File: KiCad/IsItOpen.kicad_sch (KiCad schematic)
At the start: 49 parts, among them J1 SPI Header, SW1 SW_Push, SW2 SW_Push, SW3 SW_Push, SW4 SW_Push, U1 ESP32-DevKitC, U2 MCP4801, U3 LM4562, U4 LM4871

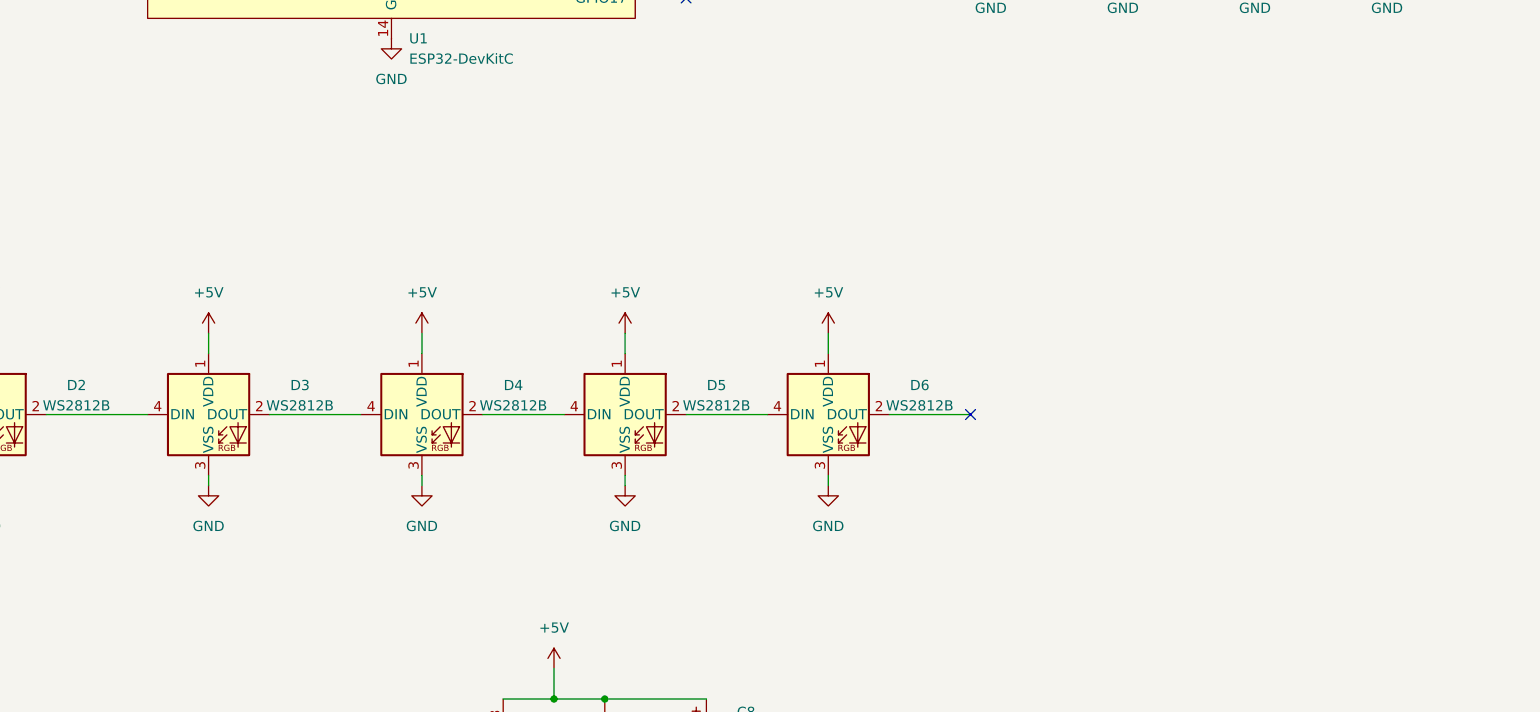
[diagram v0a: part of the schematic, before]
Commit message: added pcb connector
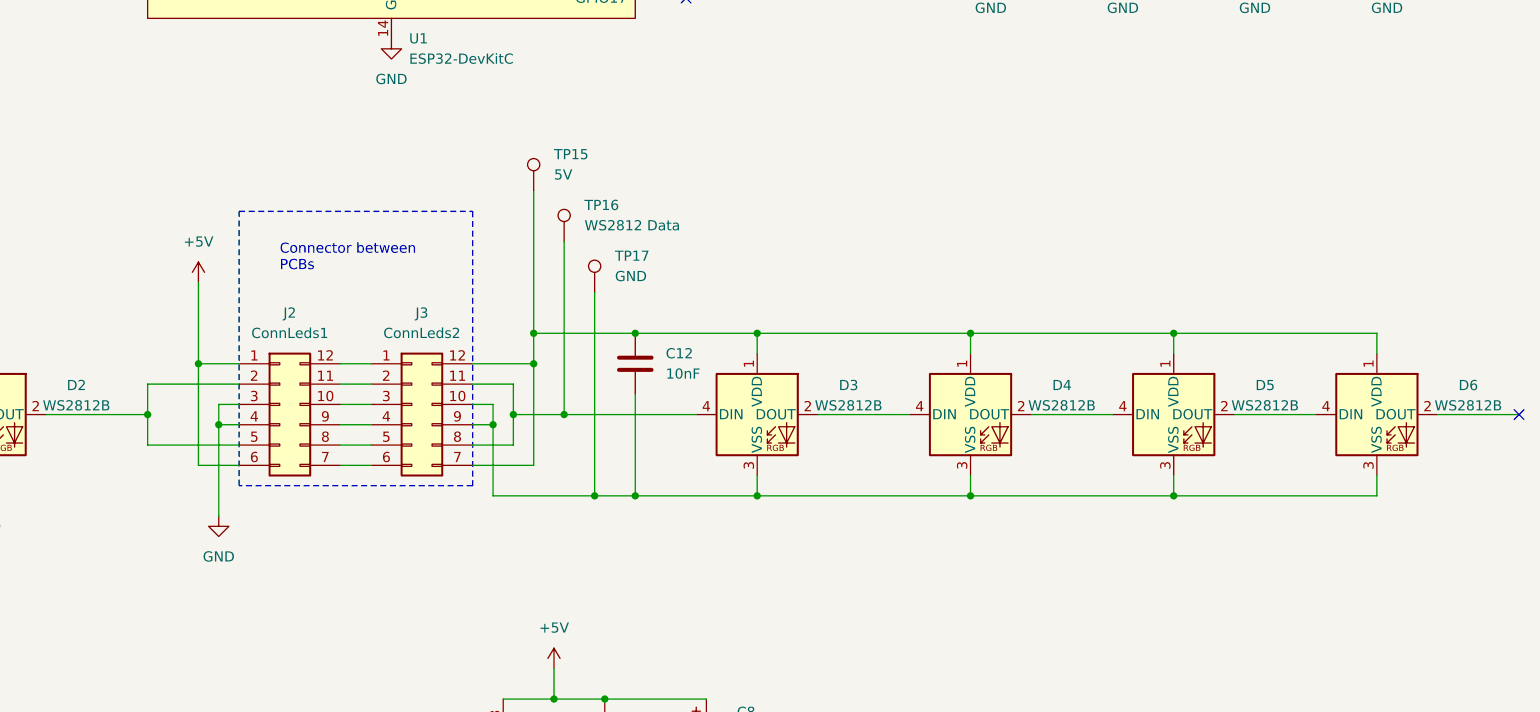
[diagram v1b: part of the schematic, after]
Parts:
- added C12: 10nF, Capacitor_SMD:C_1206_3216Metric_Pad1.33x1.80mm_HandSolder, symbol Device:C
- added J2: ConnLeds1, symbol Connector_Generic:Conn_02x06_Counter_Clockwise
- added J3: ConnLeds2, symbol Connector_Generic:Conn_02x06_Counter_Clockwise
- added TP15: 5V, TestPoint:TestPoint_Pad_D3.0mm, symbol Connector:TestPoint
- added TP16: WS2812 Data, TestPoint:TestPoint_Pad_D3.0mm, symbol Connector:TestPoint
- added TP17: GND, TestPoint:TestPoint_Pad_D3.0mm, symbol Connector:TestPoint
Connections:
- net +5V: now also J2.1 (Pin_1), J2.6 (Pin_6); no longer D3.1 (VDD), D4.1 (VDD), D5.1 (VDD), D6.1 (VDD)
- net GND: now also J2.3 (Pin_3), J2.4 (Pin_4); no longer D3.3 (VSS), D4.3 (VSS), D5.3 (VSS), D6.3 (VSS)
- net at D3.4 (DIN): now also J3.11 (Pin_11), J3.8 (Pin_8), TP16.1; no longer D2.2 (DOUT)
- new net: J2.12 (Pin_12), J3.1 (Pin_1)
- new net: C12.2, D3.3 (VSS), D4.3 (VSS), D5.3 (VSS), D6.3 (VSS), J3.10 (Pin_10), J3.9 (Pin_9), TP17.1
- new net: C12.1, D3.1 (VDD), D4.1 (VDD), D5.1 (VDD), D6.1 (VDD), J3.12 (Pin_12), J3.7 (Pin_7), TP15.1
- new net: J2.11 (Pin_11), J3.2 (Pin_2)
- new net: J2.10 (Pin_10), J3.3 (Pin_3)
- new net: J2.9 (Pin_9), J3.4 (Pin_4)
- new net: J2.8 (Pin_8), J3.5 (Pin_5)
- new net: J2.7 (Pin_7), J3.6 (Pin_6)
- new net: D2.2 (DOUT), J2.2 (Pin_2), J2.5 (Pin_5)
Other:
- note added: "Connector between PCBs"
- moved on the sheet: D3, D4, D5, D6

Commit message: added footprint for pcb connector
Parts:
- removed J2: ConnLeds1, symbol Connector_Generic:Conn_02x06_Counter_Clockwise
- removed J3: ConnLeds2, symbol Connector_Generic:Conn_02x06_Counter_Clockwise
- added J2: Base_Conn, Library:BasePCB, symbol Connector_Generic:Conn_01x06
- added J3: LED_Conn, Library:LedPCB, symbol Connector_Generic:Conn_01x06
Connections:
- net +5V: now also J2.1 (Pin_1), J2.6 (Pin_6)
- net GND: now also J2.3 (Pin_3), J2.4 (Pin_4)
- net at C12.2, D3.3 (VSS), D4.3 (VSS)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: now also J3.3 (Pin_3), J3.4 (Pin_4)
- net at D3.4 (DIN), TP16.1: now also J3.2 (Pin_2), J3.5 (Pin_5)
- net at C12.1, D3.1 (VDD), D4.1 (VDD)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: now also J3.1 (Pin_1), J3.6 (Pin_6)
- net at D2.2 (DOUT): now also J2.2 (Pin_2), J2.5 (Pin_5)
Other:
- company: (none) -> FsInf
- title: (none) -> FsInf Control

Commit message: added basic pcb layout
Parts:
- added H1, H2, H3, H4: MountingHole, MountingHole:MountingHole_3.2mm_M3, symbol Mechanical:MountingHole
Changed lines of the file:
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@@
+    )
+  )
+  (symbol (lib_id "Mechanical:MountingHole") (at 262.89 27.94 0) (unit 1)
+    (in_bom yes) (on_board yes) (dnp no) (fields_autoplaced)
+    (property "Reference" "H1" (at 265.43 26.67 0)
+      (effects (font (size 1.27 1.27)) (justify left))
+    )
+    (property "Value" "MountingHole" (at 265.43 29.21 0)
+      (effects (font (size 1.27 1.27)) (justify left))
+    )
+    (property "Footprint" "MountingHole:MountingHole_3.2mm_M3" (at 262.89 27.94 0)
+      (effects (font (size 1.27 1.27)) hide)
+    )
+    (property "Datasheet" "~" (at 262.89 27.94 0)
+      (effects (font (size 1.27 1.27)) hide)
+    )
+    (instances
+      (project "IsItOpen"
+        (path "/a8d496be-86fc-4980-841d-a8780aee3a24"
+          (reference "H1") (unit 1)
+        )
+      )
     )
   )
@@
     )
   )
+  (symbol (lib_id "Mechanical:MountingHole") (at 262.89 17.78 0) (unit 1)
+    (in_bom yes) (on_board yes) (dnp no) (fields_autoplaced)
+    (property "Reference" "H4" (at 265.43 16.51 0)
+      (effects (font (size 1.27 1.27)) (justify left))
+    )
+    (property "Value" "MountingHole" (at 265.43 19.05 0)
+      (effects (font (size 1.27 1.27)) (justify left))
+    )
+    (property "Footprint" "MountingHole:MountingHole_3.2mm_M3" (at 262.89 17.78 0)
+      (effects (font (size 1.27 1.27)) hide)
+    )
+    (property "Datasheet" "~" (at 262.89 17.78 0)
+      (effects (font (size 1.27 1.27)) hide)
+    )
+    (instances
+      (project "IsItOpen"
+        (path "/a8d496be-86fc-4980-841d-a8780aee3a24"
+          (reference "H4") (unit 1)
+        )
+      )
+    )
+  )
   (symbol (lib_id "power:GND") (at 250.19 245.11 0) (unit 1)
     (in_bom yes) (on_board yes) (dnp no) (fields_autoplaced)
@@
         (path "/a8d496be-86fc-4980-841d-a8780aee3a24"
           (reference "R3") (unit 1)
+        )
+      )
+    )
+  )
+  (symbol (lib_id "Mechanical:MountingHole") (at 262.89 33.02 0) (unit 1)
+    (in_bom yes) (on_board yes) (dnp no) (fields_autoplaced)
+    (property "Reference" "H2" (at 265.43 31.75 0)
+      (effects (font (size 1.27 1.27)) (justify left))
+    )
+    (property "Value" "MountingHole" (at 265.43 34.29 0)
+      (effects (font (size 1.27 1.27)) (justify left))
+    )
+    (property "Footprint" "MountingHole:MountingHole_3.2mm_M3" (at 262.89 33.02 0)
+      (effects (font (size 1.27 1.27)) hide)
+    )
+    (property "Datasheet" "~" (at 262.89 33.02 0)
+      (effects (font (size 1.27 1.27)) hide)
+    )
+    (instances
+      (project "IsItOpen"
+        (path "/a8d496be-86fc-4980-841d-a8780aee3a24"
+          (reference "H2") (unit 1)
         )
       )
@@
         )
       )
+    )
+  )
+  (symbol (lib_id "Mechanical:MountingHole") (at 262.89 22.86 0) (unit 1)
+    (in_bom yes) (on_board yes) (dnp no) (fields_autoplaced)
+    (property "Reference" "H3" (at 265.43 21.59 0)
+      (effects (font (size 1.27 1.27)) (justify left))
+    )
+    (property "Value" "MountingHole" (at 265.43 24.13 0)
+      (effects (font (size 1.27 1.27)) (justify left))
+    )
+    (property "Footprint" "MountingHole:MountingHole_3.2mm_M3" (at 262.89 22.86 0)
+      (effects (font (size 1.27 1.27)) hide)
+    )
+    (property "Datasheet" "~" (at 262.89 22.86 0)
+      (effects (font (size 1.27 1.27)) hide)
+    )
+    (instances
+      (project "IsItOpen"
+        (path "/a8d496be-86fc-4980-841d-a8780aee3a24"
+          (reference "H3") (unit 1)
+        )
+      )

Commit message: routed pcbn
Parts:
- added J4: Power, TerminalBlock_MetzConnect:TerminalBlock_MetzConnect_Type055_RT01502HDWU_1x02_P5.00mm_Horizontal, symbol Connector:Screw_Terminal_01x02
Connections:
- net +5V: now also J4.1 (Pin_1)
- net GND: now also J4.2 (Pin_2)
- net at J1.5 (Pin_5): now also U1.12 (MTMS/GPIO14/ADC2_CH6); no longer U1.13 (MTDI/GPIO12/ADC2_CH5)
- net at J1.6 (Pin_6): now also U1.13 (MTDI/GPIO12/ADC2_CH5); no longer U1.15 (MTCK/GPIO13/ADC2_CH4)
- net at J1.7 (Pin_7): now also U1.15 (MTCK/GPIO13/ADC2_CH4); no longer U1.12 (MTMS/GPIO14/ADC2_CH6)
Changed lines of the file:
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@@
+    (stroke (width 0) (type default))
+  )
+  (wire (pts (xy 129.54 66.04) (xy 120.65 66.04))
     (stroke (width 0) (type default))
   )
@@
     (stroke (width 0) (type default))
   )
+  (wire (pts (xy 53.34 30.48) (xy 53.34 33.02))
+    (stroke (width 0) (type default))
+  )
   (wire (pts (xy 93.98 232.41) (xy 107.95 232.41))
     (stroke (width 0) (type default))
@@
     (stroke (width 0) (type default))
   )
+  (wire (pts (xy 120.65 66.04) (xy 120.65 68.58))
+    (stroke (width 0) (type default))
+  )
   (wire (pts (xy 234.95 153.67) (xy 234.95 156.21))
     (stroke (width 0) (type default))
@@
     (stroke (width 0) (type default))
   )
+  (wire (pts (xy 123.19 68.58) (xy 123.19 60.96))
+    (stroke (width 0) (type default))
+  )
   (wire (pts (xy 177.8 163.83) (xy 184.15 163.83))
     (stroke (width 0) (type default))
@@
     (stroke (width 0) (type default))
   )
+  (wire (pts (xy 54.61 35.56) (xy 53.34 35.56))
+    (stroke (width 0) (type default))
+  )
   (wire (pts (xy 195.58 86.36) (xy 278.13 86.36))
     (stroke (width 0) (type default))
@@
     (stroke (width 0) (type default))
   )
+  (wire (pts (xy 118.11 66.04) (xy 110.49 66.04))
+    (stroke (width 0) (type default))
+  )
   (wire (pts (xy 180.34 157.48) (xy 180.34 153.67))
     (stroke (width 0) (type default))
@@
     (stroke (width 0) (type default))
   )
+  (wire (pts (xy 115.57 60.96) (xy 115.57 63.5))
+    (stroke (width 0) (type default))
+  )
   (wire (pts (xy 97.79 207.01) (xy 85.09 207.01))
     (stroke (width 0) (type default))
@@
     (stroke (width 0) (type default))
   )
+  (wire (pts (xy 120.65 68.58) (xy 110.49 68.58))
+    (stroke (width 0) (type default))
+  )
   (wire (pts (xy 177.8 160.02) (xy 177.8 163.83))
     (stroke (width 0) (type default))
   )
+  (wire (pts (xy 123.19 60.96) (xy 115.57 60.96))
+    (stroke (width 0) (type default))
+  )
+  (wire (pts (xy 53.34 33.02) (xy 54.61 33.02))
+    (stroke (width 0) (type default))
+  )
   (wire (pts (xy 163.83 224.79) (xy 153.67 224.79))
     (stroke (width 0) (type default))
@@
     (stroke (width 0) (type default))
   )
-  (wire (pts (xy 110.49 66.04) (xy 129.54 66.04))
-    (stroke (width 0) (type default))
-  )
   (wire (pts (xy 245.11 78.74) (xy 245.11 81.28))
     (stroke (width 0) (type default))
@@
     (stroke (width 0) (type default))
   )
+  (wire (pts (xy 129.54 63.5) (xy 118.11 63.5))
+    (stroke (width 0) (type default))
+  )
   (wire (pts (xy 180.34 153.67) (xy 193.04 153.67))
     (stroke (width 0) (type default))
@@
     (stroke (width 0) (type default))
   )
-  (wire (pts (xy 110.49 63.5) (xy 129.54 63.5))
-    (stroke (width 0) (type default))
-  )
   (wire (pts (xy 217.17 237.49) (xy 217.17 248.92))
     (stroke (width 0) (type default))
@@
     (stroke (width 0) (type default))
   )
+  (wire (pts (xy 115.57 63.5) (xy 110.49 63.5))
+    (stroke (width 0) (type default))
+  )
   (wire (pts (xy 119.38 163.83) (xy 132.08 163.83))
     (stroke (width 0) (type default))
@@
     (stroke (width 0) (type default))
   )
+  (wire (pts (xy 118.11 63.5) (xy 118.11 66.04))
+    (stroke (width 0) (type default))
+  )
   (wire (pts (xy 132.08 160.02) (xy 132.08 163.83))
     (stroke (width 0) (type default))
@@
     (stroke (width 0) (type default))
   )
-  (wire (pts (xy 110.49 68.58) (xy 129.54 68.58))
-    (stroke (width 0) (type default))
-  )
   (wire (pts (xy 189.23 207.01) (xy 201.93 207.01))
     (stroke (width 0) (type default))
@@
     (stroke (width 0) (type default))
   )
+  (wire (pts (xy 53.34 35.56) (xy 53.34 38.1))
+    (stroke (width 0) (type default))
+  )
   (wire (pts (xy 260.35 153.67) (xy 260.35 156.21))
+    (stroke (width 0) (type default))
+  )
+  (wire (pts (xy 129.54 68.58) (xy 123.19 68.58))
     (stroke (width 0) (type default))
   )
@@
         (path "/a8d496be-86fc-4980-841d-a8780aee3a24"
           (reference "#PWR035") (unit 1)
+        )
+      )
+    )
+  )
+  (symbol (lib_id "Connector:Screw_Terminal_01x02") (at 59.69 33.02 0) (unit 1)
+    (in_bom yes) (on_board yes) (dnp no) (fields_autoplaced)
+    (property "Reference" "J4" (at 62.23 33.02 0)
+      (effects (font (size 1.27 1.27)) (justify left))
+    )
+    (property "Value" "Power" (at 62.23 35.56 0)
+      (effects (font (size 1.27 1.27)) (justify left))
+    )
+    (property "Footprint" "TerminalBlock_MetzConnect:TerminalBlock_MetzConnect_Type055_RT01502HDWU_1x02_P5.00mm_Horizontal" (at 59.69 33.02 0)
+      (effects (font (size 1.27 1.27)) hide)
+    )
+    (property "Datasheet" "~" (at 59.69 33.02 0)
+      (effects (font (size 1.27 1.27)) hide)
+    )
+    (pin "1")
+    (pin "2")
+    (instances
+      (project "IsItOpen"
+        (path "/a8d496be-86fc-4980-841d-a8780aee3a24"
+          (reference "J4") (unit 1)
         )
       )
@@
         (path "/a8d496be-86fc-4980-841d-a8780aee3a24"
           (reference "#PWR019") (unit 1)
+        )
+      )
+    )
+  )
+  (symbol (lib_id "power:GND") (at 53.34 38.1 0) (unit 1)
+    (in_bom yes) (on_board yes) (dnp no) (fields_autoplaced)
+    (property "Reference" "#PWR026" (at 53.34 44.45 0)
+      (effects (font (size 1.27 1.27)) hide)
+    )
+    (property "Value" "GND" (at 53.34 43.18 0)
+      (effects (font (size 1.27 1.27)))
+    )
+    (property "Footprint" "" (at 53.34 38.1 0)
+      (effects (font (size 1.27 1.27)) hide)
+    )
+    (property "Datasheet" "" (at 53.34 38.1 0)
+      (effects (font (size 1.27 1.27)) hide)
+    )
+    (pin "1")
+    (instances
+      (project "IsItOpen"
+        (path "/a8d496be-86fc-4980-841d-a8780aee3a24"
+          (reference "#PWR026") (unit 1)
         )
       )
@@
         )
       )
+    )
+  )
+  (symbol (lib_id "power:+5V") (at 53.34 30.48 0) (unit 1)
+    (in_bom yes) (on_board yes) (dnp no) (fields_autoplaced)
+    (property "Reference" "#PWR025" (at 53.34 34.29 0)
+      (effects (font (size 1.27 1.27)) hide)
+    )
+    (property "Value" "+5V" (at 53.34 25.4 0)
+      (effects (font (size 1.27 1.27)))
+    )
+    (property "Footprint" "" (at 53.34 30.48 0)
+      (effects (font (size 1.27 1.27)) hide)
+    )
+    (property "Datasheet" "" (at 53.34 30.48 0)
+      (effects (font (size 1.27 1.27)) hide)
+    )
+    (pin "1")
+    (instances
+      (project "IsItOpen"
+        (path "/a8d496be-86fc-4980-841d-a8780aee3a24"
+          (reference "#PWR025") (unit 1)
+        )
+      )
